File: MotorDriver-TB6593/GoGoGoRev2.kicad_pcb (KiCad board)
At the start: 2 copper layers, 18 x 17.8 mm, 8 parts, among them P1 CONN_01X02, P2 CONN_01X04, P3 CONN_01X02, U1 TB6593FNG

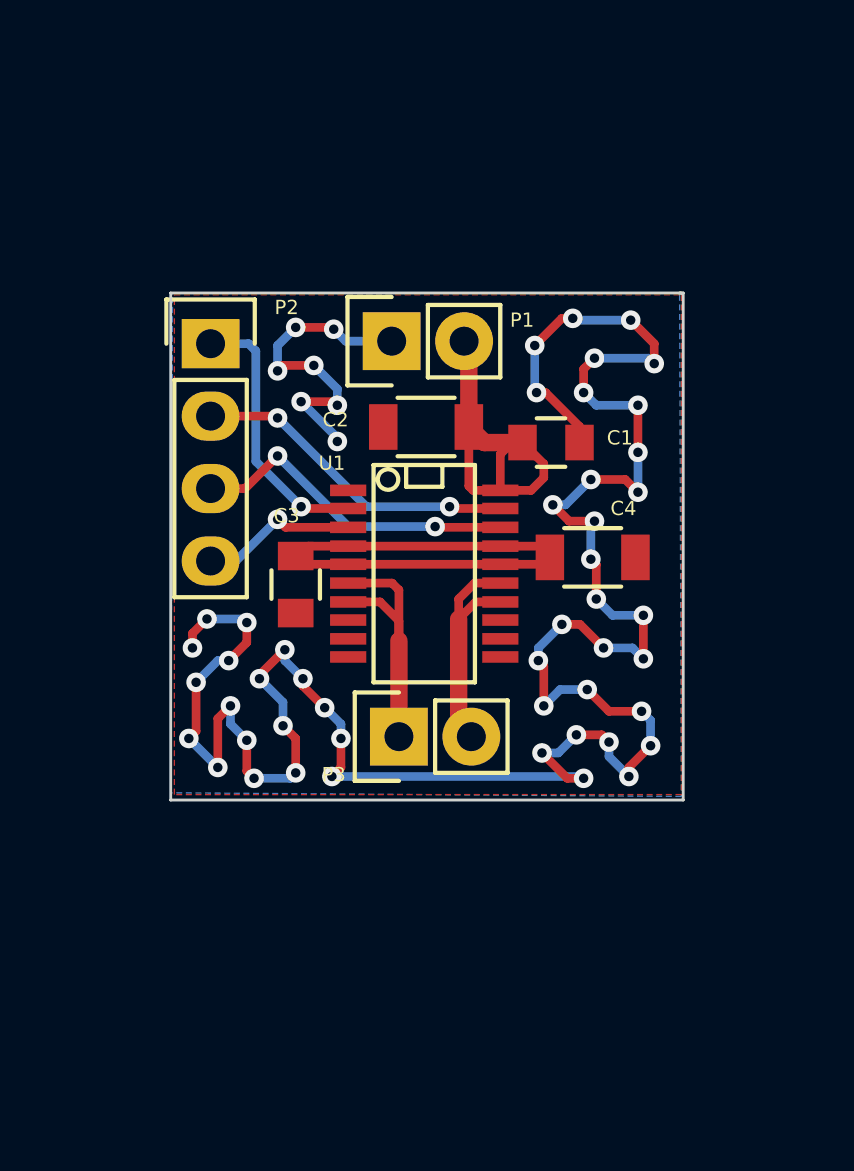
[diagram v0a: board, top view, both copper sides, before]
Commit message: Replaced parts, started redoing layout
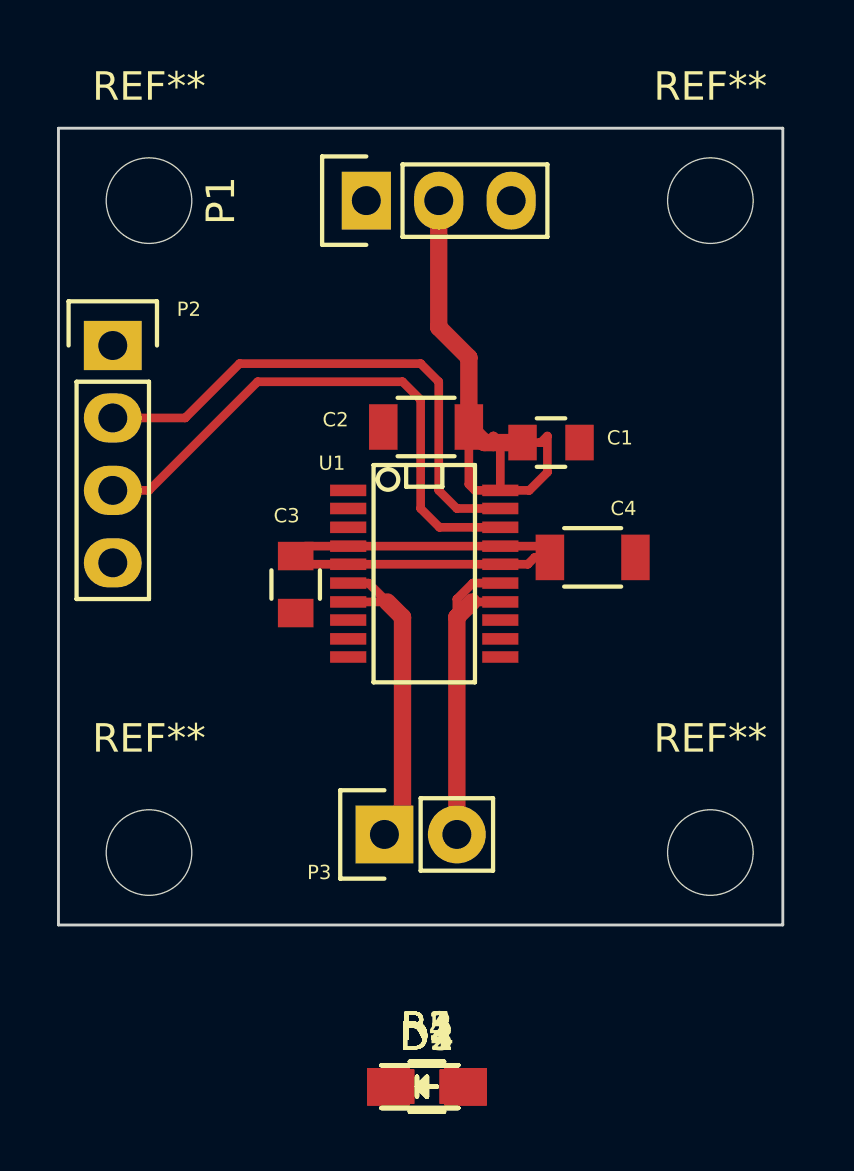
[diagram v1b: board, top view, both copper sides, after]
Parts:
- added D1, D2, D3, D4: LED, LEDs:LED-0805, F.Cu at (164.3, 138.8)
- added R1, R2, R3, R4: 1K, Resistors_SMD:R_0805_HandSoldering, F.Cu at (164.3, 138.8)
- added R5: 0, Resistors_SMD:R_0805_HandSoldering, F.Cu at (164.3, 138.8)
- added REF**: MountingHole_3mm, Mounting_Holes:MountingHole_3mm, F.Cu at (174.2, 130.6)
- added REF**: MountingHole_3mm, Mounting_Holes:MountingHole_3mm, F.Cu at (154.6, 130.6)
- added REF**: MountingHole_3mm, Mounting_Holes:MountingHole_3mm, F.Cu at (154.6, 107.7)
- added REF**: MountingHole_3mm, Mounting_Holes:MountingHole_3mm, F.Cu at (174.2, 107.7)
- P1: value CONN_01X02 -> CONN_01X03; footprint Pin_Headers:Pin_Header_Straight_1x02 -> Pin_Headers:Pin_Header_Straight_1x03
- moved P1 5.01 mm to (162.2, 107.7)
- moved P3 3.47 mm to (162.8, 129.9)
- moved P2 3.43 mm to (153.3, 112.8)
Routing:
- net GND: track 96.6 -> 0.00 mm, vias 54 -> 0
- net /PWM: track 9.49 -> 0.00 mm, vias 1 -> 0
- net /IN1: track 11.7 -> 19.5 mm, vias 2 -> 0
- net /IN2: track 11.5 -> 18.7 mm, vias 2 -> 0
- net /VCC: track 13.9 -> 20.1 mm
- net /STBY: track 5.55 -> 0.00 mm, vias 1 -> 0
- net /O2: track 8.41 -> 11.8 mm
- net /O1: track 9.77 -> 11.7 mm
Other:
- board size 18 x 17.8 mm -> 25.4 x 27.9 mm

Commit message: Finished layout, still need via stitching and DRC/DFM checks
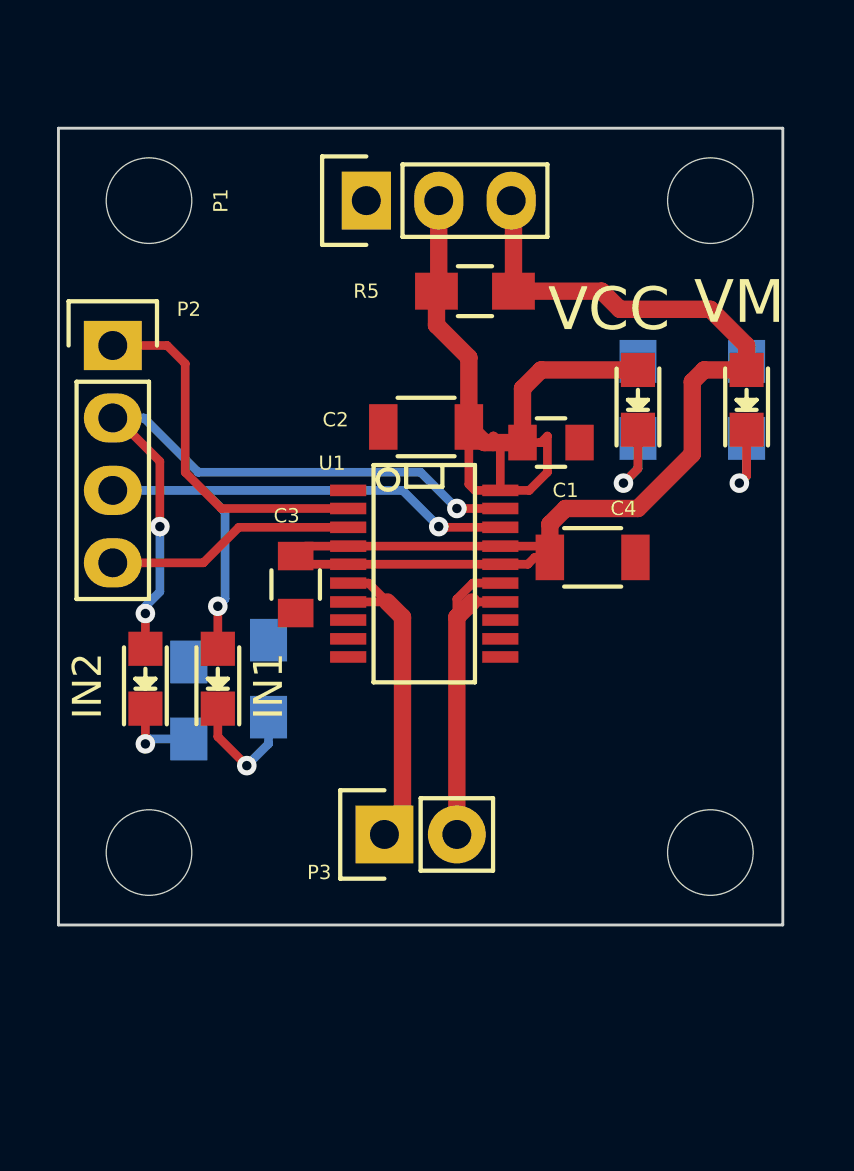
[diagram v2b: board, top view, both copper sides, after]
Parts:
- R1, R2, R3, R4: moved to B.Cu
- moved R5 27.9 mm to (166.0, 110.9), turned to 180 degrees
- moved D1 26.6 mm to (175.5, 114.7), turned to 90 degrees
- moved R1 26.6 mm to (175.5, 114.7), turned to 270 degrees
- moved D2 25.2 mm to (171.7, 114.7), turned to 90 degrees
- moved R2 25.2 mm to (171.7, 114.7), turned to 270 degrees
- moved D4 17.4 mm to (154.4, 124.5), turned to 90 degrees
- moved D3 16.1 mm to (157.0, 124.5), turned to 90 degrees
- moved R4 15.9 mm to (156.0, 125.2), turned to 270 degrees
- moved R3 15.3 mm to (158.8, 124.5), turned to 270 degrees
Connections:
- D2 pad 2: /VM -> /VCC
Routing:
- net /VM: track 18.4 -> 43.2 mm
- net /PWM: track 0.00 -> 12.9 mm
- net /STBY: track 0.00 -> 8.77 mm
- net /VCC: track 20.1 -> 26.4 mm
- net /IN2: track 18.7 -> 24.0 mm, vias 0 -> 3
- net Net-(D3-Pad1): track 0.00 -> 4.43 mm, vias 0 -> 1
- net Net-(D2-Pad1): track 0.00 -> 3.86 mm, vias 0 -> 1
- net Net-(D1-Pad1): track 0.00 -> 3.65 mm, vias 0 -> 1
- net Net-(D4-Pad1): track 0.00 -> 2.83 mm, vias 0 -> 1
- net /IN1: track 19.5 -> 20.1 mm, vias 0 -> 2
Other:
- board text added: "IN1"
- board text added: "IN2"
- board text added: "VCC"
- board text added: "VM"
